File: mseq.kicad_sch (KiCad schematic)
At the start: 81 parts, among them J1 Screen_I2C, J3 Conn_ARM_JTAG_SWD_10, SW1 RESET, SW2 ON/OFF, SW3 MS/SLAVE, SW4 BOOT, U1 SN74AHCT125DR, U2 H11L1M, U3 MCP1703Ax-330xxTT, U4 STM32F413CHUx, U5 CP2102N-Axx-xQFN20, U6 H11L1M, Y1 32.768kHz ±20ppm 6pF, Y2 25 MHz ±20ppm 18pF

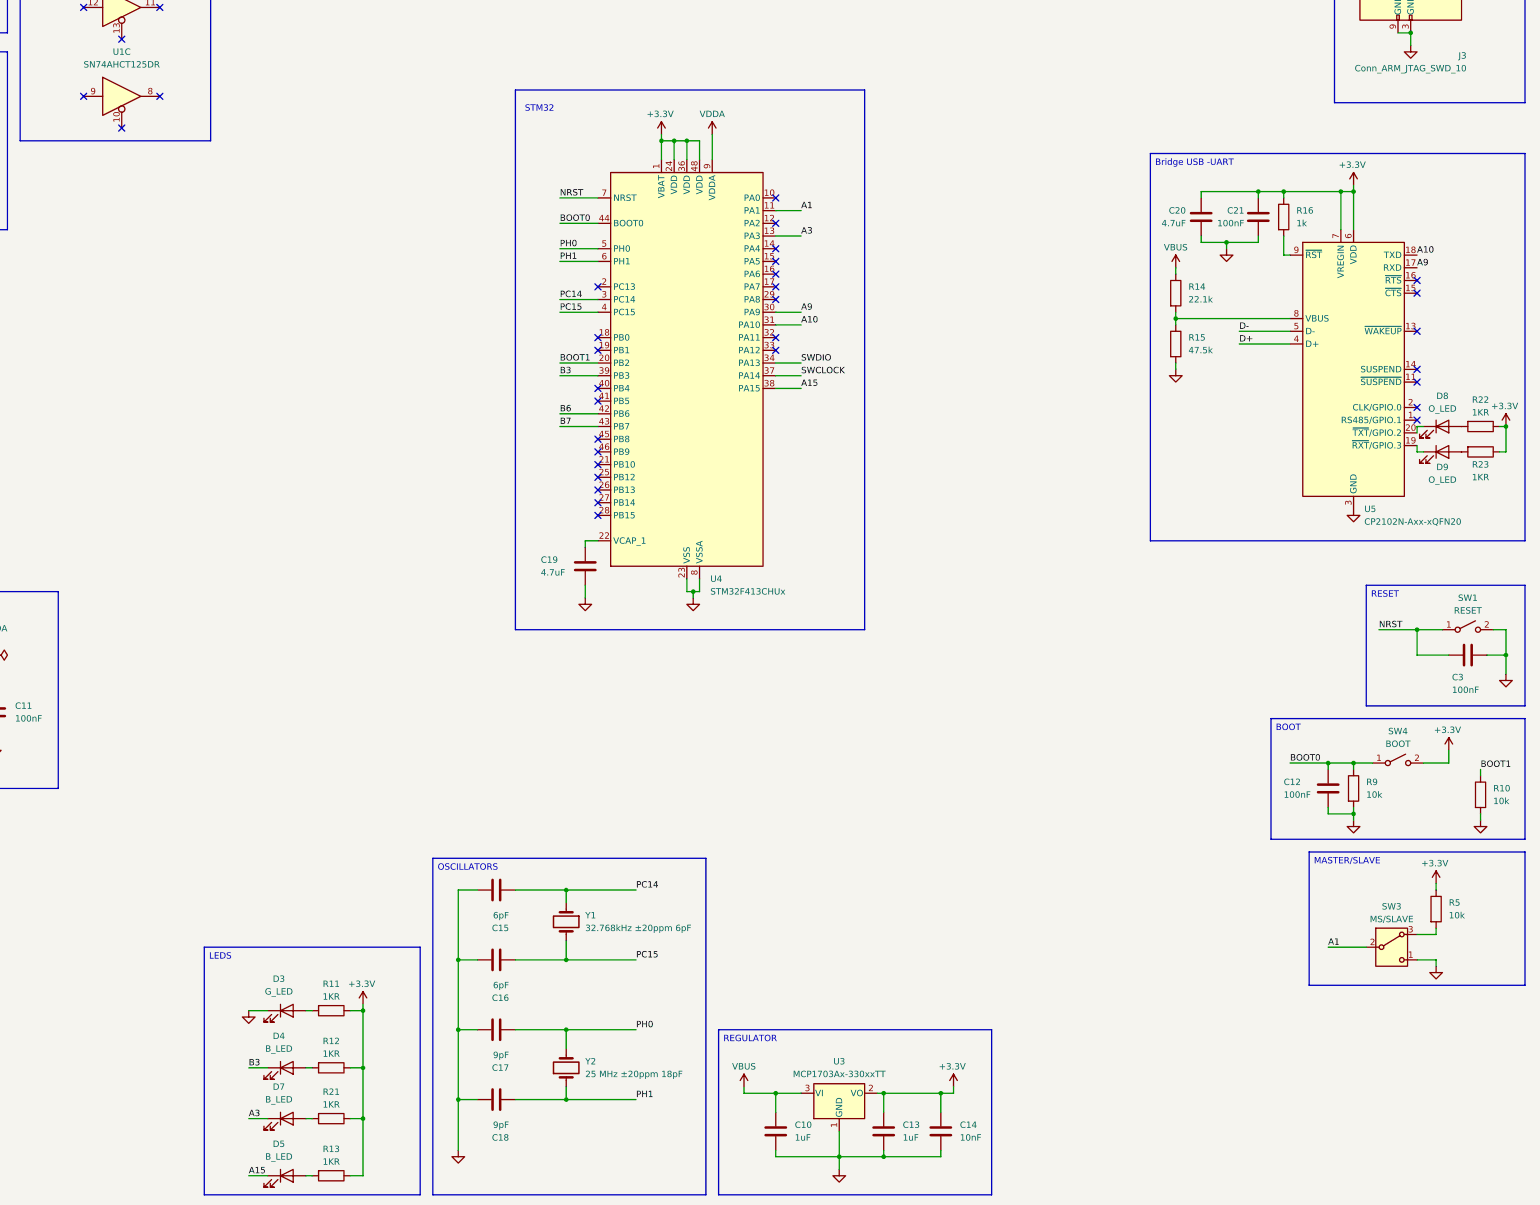
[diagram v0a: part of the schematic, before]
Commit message: NOR Flash added wip
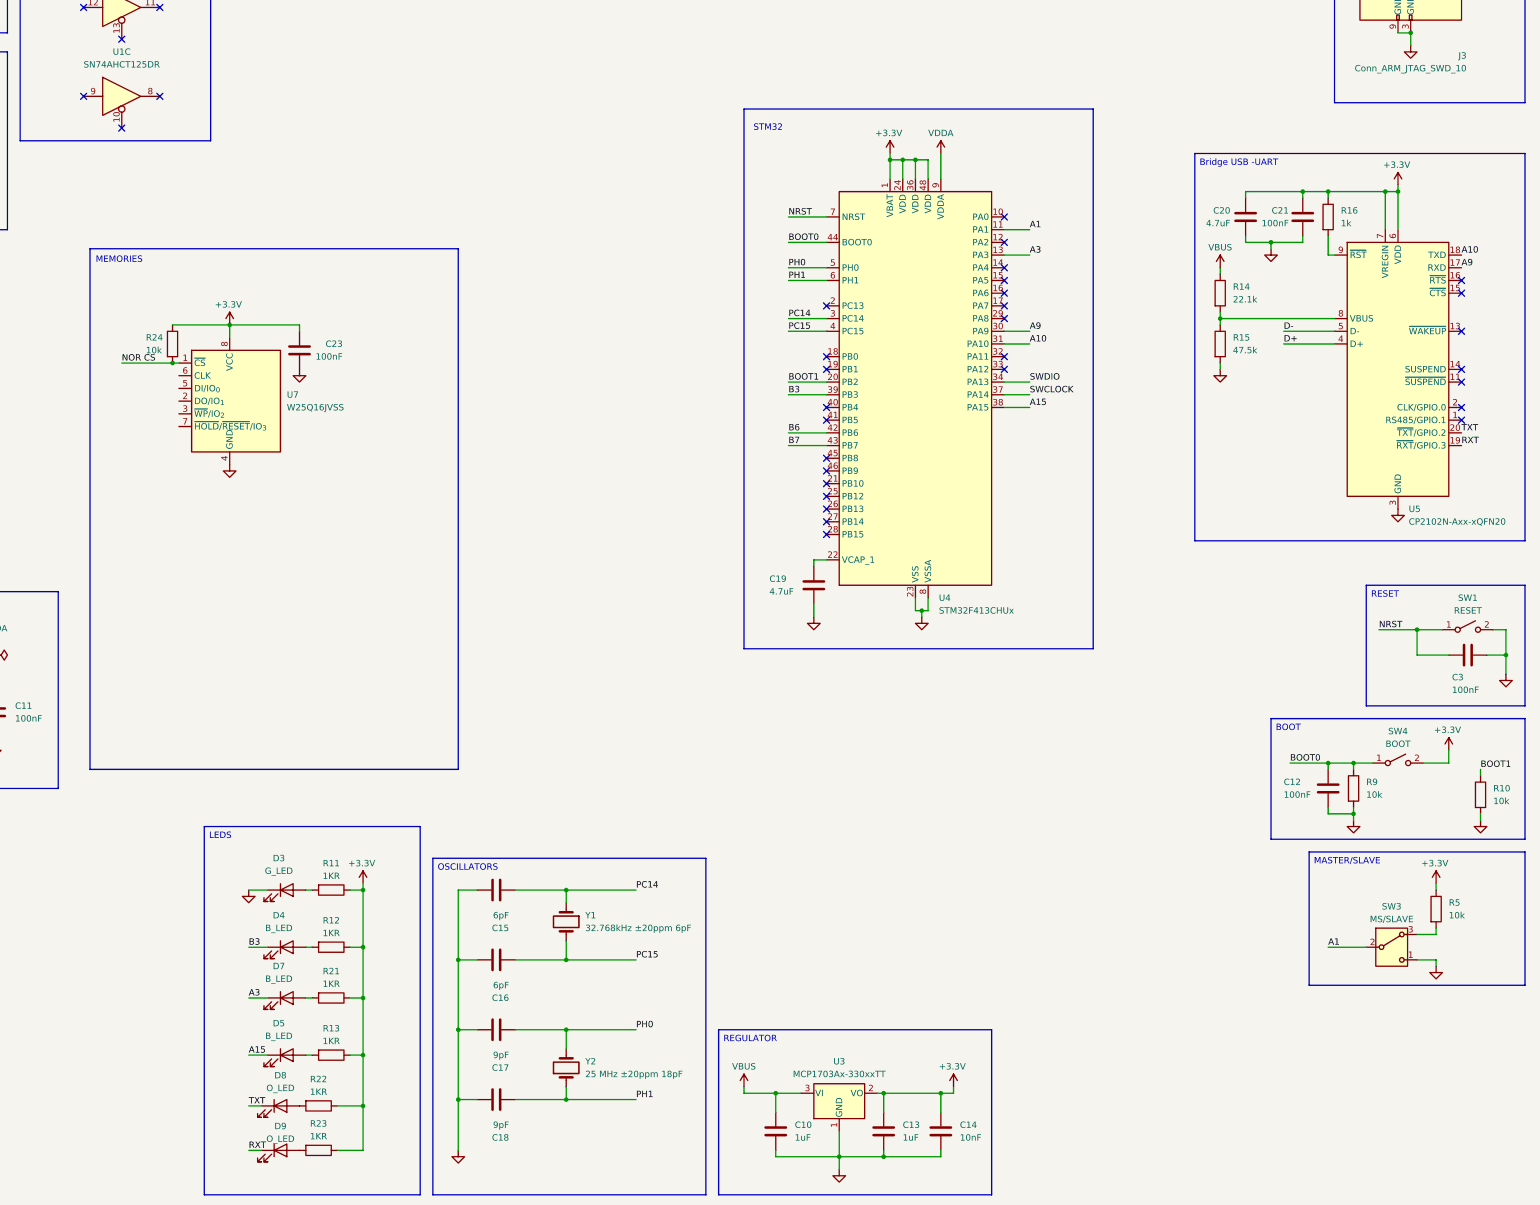
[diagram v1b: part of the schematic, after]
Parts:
- added C23: 100nF, Capacitor_SMD:C_0603_1608Metric, symbol Device:C
- added R24: 10k, Resistor_SMD:R_0603_1608Metric, symbol Device:R
- added U7: W25Q16JVSS, Package_SO:SOIC-8_5.3x5.3mm_P1.27mm, symbol Memory_Flash:W25Q16JVSS
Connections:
- net +3.3V: now also C23.2, R24.1, U7.8 (VCC)
- net GND: now also C23.1, U7.4 (GND)
- net TXT: now reaches D8.1 (K), U5.20 (~{TXT}/GPIO.2)
- net RXT: now reaches D9.1 (K), U5.19 (~{RXT}/GPIO.3)
- new net NOR CS: R24.2, U7.1 (~{CS})
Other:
- note added: "MEMORIES"
- moved on the sheet: C19, C20, C21, D3, D4, D5, D7, R11, R12, R13, R14, R15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
